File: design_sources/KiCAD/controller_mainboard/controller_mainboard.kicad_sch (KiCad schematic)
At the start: 2 parts, among them J5 XT-90, J6 USB_C_Receptacle_USB2.0_16P

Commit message: Commit after closing kicad
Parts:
- added L4: 5A 1uH, symbol Device:L
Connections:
- net at J6.A6 (D+): now also J6.B6 (D+)
- net at J6.A7 (D-): now also J6.B7 (D-)
- net at J6.S1 (SHIELD): now also L4.1
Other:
- note added: "22R resistors and MAKE THIS DIFFERENTIAL"
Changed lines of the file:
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@@
+		)
+	)
+	(text "22R resistors and MAKE THIS DIFFERENTIAL\n"
+		(exclude_from_sim no)
+		(at 59.436 118.11 0)
+		(effects
+			(font
+				(size 1.27 1.27)
+			)
+			(justify left top)
+		)
+	)
+	(wire
+		(pts
+			(xy 45.72 142.24) (xy 45.72 144.78)
+		)
+		(stroke
+			(width 0)
+			(type default)
+		)
+	)
+	(wire
+		(pts
+			(xy 45.72 144.78) (xy 43.18 144.78)
+		)
+		(stroke
+			(width 0)
+			(type default)
+		)
+	)
+	(wire
+		(pts
+			(xy 43.18 124.46) (xy 57.15 124.46)
+		)
+		(stroke
+			(width 0)
+			(type default)
+		)
+	)
+	(wire
+		(pts
+			(xy 20.32 173.99) (xy 21.59 173.99)
+		)
+		(stroke
+			(width 0)
+			(type default)
+		)
+	)
+	(wire
+		(pts
+			(xy 45.72 139.7) (xy 45.72 137.16)
+		)
+		(stroke
+			(width 0)
+			(type default)
+		)
+	)
+	(wire
+		(pts
+			(xy 20.32 162.56) (xy 20.32 173.99)
+		)
+		(stroke
+			(width 0)
+			(type default)
+		)
+	)
+	(wire
+		(pts
+			(xy 45.72 137.16) (xy 43.18 137.16)
+		)
+		(stroke
+			(width 0)
+			(type default)
+		)
+	)
+	(wire
+		(pts
+			(xy 43.18 142.24) (xy 45.72 142.24)
+		)
+		(stroke
+			(width 0)
+			(type default)
+		)
+	)
+	(wire
+		(pts
+			(xy 43.18 139.7) (xy 45.72 139.7)
+		)
+		(stroke
+			(width 0)
+			(type default)
+		)
+	)
+	(symbol
+		(lib_id "Device:L")
+		(at 25.4 173.99 90)
+		(unit 1)
+		(exclude_from_sim no)
+		(in_bom yes)
+		(on_board yes)
+		(dnp no)
+		(fields_autoplaced yes)
+		(property "Reference" "L4"
+			(at 25.4 168.91 90)
+			(effects
+				(font
+					(size 1.27 1.27)
+				)
+			)
+		)
+		(property "Value" "5A 1uH"
+			(at 25.4 171.45 90)
+			(effects
+				(font
+					(size 1.27 1.27)
+				)
+			)
+		)
+		(property "Footprint" ""
+			(at 25.4 173.99 0)
+			(effects
+				(font
+					(size 1.27 1.27)
+				)
+				(hide yes)
+			)
+		)
+		(property "Datasheet" "~"
+			(at 25.4 173.99 0)
+			(effects
+				(font
+					(size 1.27 1.27)
+				)
+				(hide yes)
+			)
+		)
+		(property "Description" "Inductor"
+			(at 25.4 173.99 0)
+			(effects
+				(font
+					(size 1.27 1.27)
+				)
+				(hide yes)
+			)
+		)
+		(property "JLCPCB" "C167953"
+			(at 25.4 173.99 90)
+			(effects
+				(font
+					(size 1.27 1.27)
+				)
+				(hide yes)
+			)
+		)
+		(pin "1"
+		)
+		(pin "2"
+		)
+		(instances
+			(project "controller_mainboard"
+				(path "/0fdfffec-3d24-4249-8ba9-dae7a6ccc250"
+					(reference "L4")
+					(unit 1)
+				)
+			)
 		)
 	)
@@
 	)
 	(sheet
-		(at 73.66 95.25)
+		(at 76.2 127)
 		(size 33.02 35.56)
 		(exclude_from_sim no)
@@
 		)
 		(property "Sheetname" "ATmega16u2"
-			(at 73.66 94.5384 0)
+			(at 76.2 126.2884 0)
 			(effects
 				(font
@@
 		)
 		(property "Sheetfile" "atmega16u2_schematic.kicad_sch"
-			(at 73.66 131.3946 0)
+			(at 76.2 163.1446 0)
 			(effects
 				(font
@@
 		)
 		(pin "PE0" output
-			(at 106.68 111.76 0)
+			(at 109.22 143.51 0)
 			(effects
 				(font
@@
 		)
 		(pin "PE1" output
-			(at 106.68 114.3 0)
+			(at 109.22 146.05 0)
 			(effects
 				(font
@@
 		)
 		(pin "RESET_CPL" input
-			(at 106.68 125.73 0)
+			(at 109.22 157.48 0)
 			(effects
 				(font
@@
 		)
 		(pin "usb_d+" input
-			(at 73.66 114.3 180)
+			(at 76.2 146.05 180)
 			(effects
 				(font
@@
 		)
 		(pin "usb_d-" input
-			(at 73.66 116.84 180)
+			(at 76.2 148.59 180)
 			(effects
 				(font
@@
 		)
 		(pin "usb_GND" passive
-			(at 73.66 119.38 180)
+			(at 76.2 151.13 180)
 			(effects
 				(font
@@
 		)
 		(pin "usb_VCC" input
-			(at 73.66 111.76 180)
-			(effects
-				(font
+			(at 76.2 143.51 180)
+			(effects
+				(font

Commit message: Populated the schematic more, added buck.
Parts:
- removed L4: 5A 1uH, symbol Device:L
- added D12: 40V 5A, Diode_SMD:D_SMA, symbol Device:D
- added D13: LED RED, LED_SMD:LED_0603_1608Metric, symbol Device:LED
- added F1: Fuse 20A, Custom_feetprint:BLX-A fuse holder, symbol Device:Fuse
- added FB1: GZ2012D101TF, Inductor_SMD:L_0805_2012Metric, symbol Device:FerriteBead
- added J10, J11, J8, J9: 2P_screw_term, symbol Connector_Generic:Conn_01x02
- added J7: XT-60, symbol Connector_Generic:Conn_01x02
- added Q5: 2N7002, Package_TO_SOT_SMD:SOT-23, symbol Transistor_FET:2N7002
- added R17, R18: 22R 100mW, Resistor_SMD:R_0603_1608Metric, symbol Device:R
- added R23: 10k 63mW, Resistor_SMD:R_0402_1005Metric, symbol Device:R
- added R24: 1k 63mW, Resistor_SMD:R_0402_1005Metric, symbol Device:R
- added R26, R27: 5.1K 100mW, Capacitor_SMD:C_0603_1608Metric, symbol Device:R
- added SW1: SW_SPDT, Custom_feetprint:MTS-10x, symbol Switch:SW_SPDT
- J6: footprint (none) -> Connector_USB:USB_C_Receptacle_GCT_USB4105-xx-A_16P_TopMnt_Horizontal; JLCPCB (none) -> C2927038
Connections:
- net at J6.S1 (SHIELD): now also FB1.1
- net at J5.1 (Pin_1): now also F1.2, J7.1 (Pin_1), R24.2
- net GND: now reaches J5.2 (Pin_2)
- net GND: now also J7.2 (Pin_2), Q5.2 (S), R23.1
- net USB_GND: now reaches J6.A1 (GND), J6.A12 (GND), J6.B1 (GND), J6.B12 (GND)
- net USB_GND: now also FB1.2, R26.2, R27.2
- net USB_VBUS: now reaches J6.A4 (VBUS), J6.A9 (VBUS), J6.B4 (VBUS), J6.B9 (VBUS)
- net USB_VBUS: now also D12.2 (A), Q5.1 (G), R23.2
- net at J6.A5 (CC1): now also R27.1
- net USB_DATA_P: now reaches J6.A6 (D+), J6.B6 (D+)
- net USB_DATA_P: now also R18.2
- net USB_DATA_N: now reaches J6.A7 (D-), J6.B7 (D-)
- net USB_DATA_N: now also R17.2
- net at J6.B5 (CC2): now also R26.1
- new net: F1.1, SW1.2 (B)
- new net: D13.2 (A), R24.1
- new net +5V: D12.1 (K)
- new net +BATT: D13.1 (K), SW1.3 (C)
- new net 5V_3A_buck_converter/BUCK_EN: Q5.3 (D)
- new net Motor driver 1/MOTOR_A: J8.1 (Pin_1)
- new net Motor driver 1/MOTOR_B: J8.2 (Pin_2)
- new net Motor driver 2/MOTOR_A: J9.1 (Pin_1)
- new net Motor driver 2/MOTOR_B: J9.2 (Pin_2)
- new net Motor driver 3/MOTOR_A: J10.1 (Pin_1)
- new net Motor driver 3/MOTOR_B: J10.2 (Pin_2)
- new net Motor driver 4/MOTOR_A: J11.1 (Pin_1)
- new net Motor driver 4/MOTOR_B: J11.2 (Pin_2)
- new net USB_D_N: R17.1
- new net USB_D_P: R18.1
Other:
- removed sheet Motor driver
- added sheet 5V_3A_buck_converter (5V5_36V_3A_buck_converter_5V.kicad_sch)
- added sheet Motor driver 1 (dc_motor_driver.kicad_sch)
- added sheet Motor driver 2 (dc_motor_driver.kicad_sch)
- added sheet Motor driver 3 (dc_motor_driver.kicad_sch)
- added sheet Motor driver 4 (dc_motor_driver.kicad_sch)
- note added: "0.8A, 100Ohm@100MHz, Rdc 150mOhm"
- note added: "5A*4 = 20A"
- note added: "CC conf marks USB2.0"
- note added: "Disable buck when usb connected"
- note added: "FLT indicator"
- note added: "Supply range: 8.5V - 15"
- note removed: "22R resistors and MAKE THIS DIFFERENTIAL"
- moved on the sheet: J5

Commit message: Continued development on the schematic. Pins wired. TODO validate.
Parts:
- added J13: 02x20_raspbi_conn, symbol Connector_Generic:Conn_02x20_Odd_Even
- added J14: Conn_01x10_2.54mm_socket, Connector_PinSocket_2.54mm:PinSocket_1x10_P2.54mm_Vertical, symbol Connector:Conn_01x10_Socket
- added J15, J17, J21, J22, J23: 01x08_2.54mm _socket, Connector_PinSocket_2.54mm:PinSocket_1x08_P2.54mm_Vertical, symbol Connector:Conn_01x08_Socket
- added J18: 02x18_2.54mm_socket, symbol Connector_Generic:Conn_02x18_Odd_Even
- added Q6: 2N7002, Package_TO_SOT_SMD:SOT-23, symbol Transistor_FET:2N7002
- added R25: 10k 63mW, Resistor_SMD:R_0402_1005Metric, symbol Device:R
- added R28: 22R 100mW, Resistor_SMD:R_0603_1608Metric, symbol Device:R
- J10, J11, J9: footprint (none) -> Connector_JST:JST_NV_B02P-NV_1x02_P5.00mm_Vertical
- J8: footprint (none) -> Connector_JST:JST_NV_B02P-NV_1x02_P5.00mm_Vertical; tinytronics (none) -> https://www.tinytronics.nl/en/cables-and-connectors/connect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
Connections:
- net +5V: now also J15.2 (Pin_2), J15.5 (Pin_5), J18.1 (Pin_1), J18.2 (Pin_2)
- net 5V_3A_buck_converter/BUCK_EN: now also Q6.3 (D)
- net GND: now also J13.14 (Pin_14), J13.20 (Pin_20), J13.25 (Pin_25), J13.30 (Pin_30), J13.34 (Pin_34), J13.39 (Pin_39), J13.6 (Pin_6), J13.9 (Pin_9), J14.4 (Pin_4), J15.6 (Pin_6), J15.7 (Pin_7), J18.35 (Pin_35), J18.36 (Pin_36), Q6.2 (S), R25.1
- new net: Q6.1 (G), R25.2, R28.1
- new net +3V3: J13.1 (Pin_1), J13.17 (Pin_17), J15.4 (Pin_4), R28.2
- new net ADC0: J21.1 (Pin_1)
- new net ADC1: J21.2 (Pin_2)
- new net ADC10: J17.3 (Pin_3)
- new net ADC11: J17.4 (Pin_4)
- new net ADC12: J17.5 (Pin_5)
- new net ADC13: J17.6 (Pin_6)
- new net ADC14: J17.7 (Pin_7)
- new net ADC15: J17.8 (Pin_8)
- new net ADC2: J21.3 (Pin_3)
- new net ADC3: J21.4 (Pin_4)
- new net ADC4: J21.5 (Pin_5)
- new net ADC5: J21.6 (Pin_6)
- new net ADC6: J21.7 (Pin_7)
- new net ADC7: J21.8 (Pin_8)
- new net ADC8: J17.1 (Pin_1)
- new net ADC9: J17.2 (Pin_2)
- new net AREF: J14.3 (Pin_3)
- new net D0: J23.8 (Pin_8)
- new net D1: J23.7 (Pin_7)
- new net D10: J14.8 (Pin_8)
- new net D11: J14.7 (Pin_7)
- new net D12: J14.6 (Pin_6)
- new net D13: J14.5 (Pin_5)
- new net D14: J22.1 (Pin_1)
- new net D15: J22.2 (Pin_2)
- new net D16: J22.3 (Pin_3)
- new net D17: J22.4 (Pin_4)
- new net D18: J22.5 (Pin_5)
- new net D19: J22.6 (Pin_6)
- new net D2: J23.6 (Pin_6)
- new net D20: J14.2 (Pin_2), J22.7 (Pin_7)
- new net D21: J14.1 (Pin_1), J22.8 (Pin_8)
- new net D22: J18.3 (Pin_3)
- new net D23: J18.4 (Pin_4)
- new net D24: J18.5 (Pin_5)
- new net D25: J18.6 (Pin_6)
- new net D26: J18.7 (Pin_7)
- new net D27: J18.8 (Pin_8)
- new net D28: J18.9 (Pin_9)
- new net D29: J18.10 (Pin_10)
- new net D3: J23.5 (Pin_5)
- new net D30: J18.11 (Pin_11)
- new net D31: J18.12 (Pin_12)
- new net D32: J18.13 (Pin_13)
- new net D33: J18.14 (Pin_14)
- new net D34: J18.15 (Pin_15)
- new net D35: J18.16 (Pin_16)
- new net D36: J18.17 (Pin_17)
- new net D37: J18.18 (Pin_18)
- new net D38: J18.19 (Pin_19)
- new net D39: J18.20 (Pin_20)
- new net D4: J23.4 (Pin_4)
- new net D40: J18.21 (Pin_21)
- new net D41: J18.22 (Pin_22)
- new net D42: J18.23 (Pin_23)
- new net D43: J18.24 (Pin_24)
- new net D44: J18.25 (Pin_25)
- new net D45: J18.26 (Pin_26)
- new net D46: J18.27 (Pin_27)
- new net D47: J18.28 (Pin_28)
- new net D48: J18.29 (Pin_29)
- new net D49: J18.30 (Pin_30)
- new net D5: J23.3 (Pin_3)
- new net D50: J18.31 (Pin_31)
- new net D51: J18.32 (Pin_32)
- new net D52: J18.33 (Pin_33)
- new net D53: J18.34 (Pin_34)
- new net D6: J23.2 (Pin_2)
- new net D7: J23.1 (Pin_1)
- new net D8: J14.10 (Pin_10)
- new net D9: J14.9 (Pin_9)
- new net RPI_GPIO0: J13.27 (Pin_27)
- new net RPI_GPIO1: J13.28 (Pin_28)
- new net RPI_GPIO10: J13.19 (Pin_19)
- new net RPI_GPIO11: J13.23 (Pin_23)
- new net RPI_GPIO12: J13.32 (Pin_32)
- new net RPI_GPIO13: J13.33 (Pin_33)
- new net RPI_GPIO14: J13.8 (Pin_8)
- new net RPI_GPIO15: J13.10 (Pin_10)
- new net RPI_GPIO16: J13.36 (Pin_36)
- new net RPI_GPIO17: J13.11 (Pin_11)
- new net RPI_GPIO18: J13.12 (Pin_12)
- new net RPI_GPIO19: J13.35 (Pin_35)
- new net RPI_GPIO2: J13.3 (Pin_3)
- new net RPI_GPIO20: J13.38 (Pin_38)
- new net RPI_GPIO21: J13.40 (Pin_40)
- new net RPI_GPIO22: J13.15 (Pin_15)
- new net RPI_GPIO23: J13.16 (Pin_16)
- new net RPI_GPIO24: J13.18 (Pin_18)
- new net RPI_GPIO25: J13.22 (Pin_22)
- new net RPI_GPIO26: J13.37 (Pin_37)
- new net RPI_GPIO27: J13.13 (Pin_13)
- new net RPI_GPIO3: J13.5 (Pin_5)
- new net RPI_GPIO4: J13.7 (Pin_7)
- new net RPI_GPIO5: J13.29 (Pin_29)
- new net RPI_GPIO6: J13.31 (Pin_31)
- new net RPI_GPIO7: J13.26 (Pin_26)
- new net RPI_GPIO8: J13.24 (Pin_24)
- new net RPI_GPIO9: J13.21 (Pin_21)
- new net ~{mega2560_reset}: J15.3 (Pin_3)
- no-connect marks 0 -> 2
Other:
- added sheet Quadrature encoder 1 (qdec_pullup.kicad_sch)
- added sheet Quadrature encoder 2 (qdec_pullup.kicad_sch)
- added sheet Quadrature encoder 3 (qdec_pullup.kicad_sch)
- added sheet Quadrature encoder 4 (qdec_pullup.kicad_sch)
- sheet atmega2560 ports: added ADC0, ADC1, ADC10, ADC11, ADC12, ADC13, ADC14, ADC15, ADC2, ADC3, ADC4, ADC5, ADC6, ADC7, ADC8, ADC9, AREF, PA0/D22, PA1/D23, PA2/D24, PA3/D25, PA4/D26, PA5/D27, PA6/D28, PA7/D29, PB0/D55/SS, PB1/D52/SCK, PB2/D51/MOSI, PB3/D50/MISO, PB4/D10, PB5/D11, PB6/D12, PB7/D13, PC0/D37, PC1/D36, PC2/D35, PC3/D34, PC4/D33, PC5/D32, PC6/D31, PC7/D30, PD0/D21/SCL, PD1/D20/SDA, PD2/D19/RXD1, PD3/D18/TXD1, PD7/D38, PE0/D0/RX0, PE1/D1/TX0, PE3/D5, PE4/D2, PE5/D3, PG0/D41, PG1/D40, PG2/D39, PG5/D4, PH0/D17/RXD2, PH1/D16/TXD2, PH3/D6, PH4/D7, PH5/D8, PH6/D9, PL0/D49, PL1/D48, PL2/D47, PL3/D46, PL4/D45, PL5/D44, PL6/D43, PL7/D42, RXD3, TXD3, ~{RESET}; removed none
- note added: "All raspbi after B+ can provide up to 500mA on 3v3."
- note added: "Didn't the TETRIX motor have JST? They have a 2mm pitch jst type connector. Probably PH The motor has 4P male side."
- note added: "Does rasbpi want to PWM control?"
- note added: "FLT/OPEN indicator"
- note added: "Get these from Tinytronics to interface the encoders with the PCB: JST-PH Female to DuPont Female Compatible Cable - 4p - 15cm SKU:005974 https://www.tinytronics.nl/en/cables-and-connectors/cables-and-adapters/jst-compatible/jst-ph-female-to-dupont-female-compatible-cable-4p-15cm"
- note added: "Raspi 5V supply"
- note added: "TODO VALIDATE"
- note added: "TODO, check if we can change this flag into something like V_PERIPHERAL So that it can be swapped with 5V or 3V3"
- note added: "TODOS - CHECK if 5v buck can handle external 5v supply while disabled. - place esd parts - Selectable peripheral voltage 3.3V/5V for enc control"
- note removed: "FLT indicator"
- company: Kestech -> Mete Han Keskin
- moved on the sheet: D12, FB1, J10, J11, J6, J8, J9, Q5, R17, R18, R23, R26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

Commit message: Added ESD protection ic, added footprints to all IC and loaded into pcbnew to size up the pcb size.
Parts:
- added U12: USBLC6-4SC6, Package_TO_SOT_SMD:SOT-23-6, symbol Power_Protection:USBLC6-4SC6
- J1: renamed from J5; footprint (none) -> Custom_feetprint:XT-90_Connector
- J15: renamed from J13; footprint (none) -> Connector_PinHeader_2.54mm:PinHeader_2x20_P2.54mm_Vertical
- J2: renamed from J7; footprint (none) -> Connector_AMASS:AMASS_XT60-M_1x02_P7.20mm_Vertical
- J7: renamed from J18; footprint (none) -> Connector_PinHeader_2.54mm:PinHeader_2x18_P2.54mm_Vertical
- renumbered D13 to D1, D12 to D2, J22 to J10, J8 to J11, J9 to J12, J10 to J13, J11 to J14, J6 to J3, J15 to J4, J21 to J5, J17 to J6, J14 to J8, J23 to J9, Q5 to Q1, Q6 to Q2, R23 to R1, R28 to R2, R25 to R3, R24 to R4, R27 to R5, R26 to R6, R17 to R7, R18 to R8
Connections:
- net USB_DATA_N: now also U12.3 (I/O2)
- net USB_DATA_P: now also U12.1 (I/O1)
- net USB_GND: now also U12.2 (GND)
- net USB_VBUS: now also U12.5 (VBUS)
- net at J3.B5 (CC2), R6.1: now also U12.4 (I/O3)
- net at J3.A5 (CC1), R5.1: now also U12.6 (I/O4)
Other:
- note added: "ESD stuff DFN1006 single C22395519 LSR05-TP C779191 HELL YEAh C778952 mex dfn16"
- note added: "PERFECT!!! USBLC6-4SC6-ES C5180279 SEUC10F5V4U C5126804 IP4220CZ6-ES C5199235"
- note added: "Single channel esd protect ESD5V0AP C5199224"
- moved on the sheet: D2, FB1, J10, J11, J12, J13, J14, J4, J5, J6, J7, J8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

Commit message: Read through schematic to bugfix.
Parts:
- removed Q2: 2N7002, Package_TO_SOT_SMD:SOT-23, symbol Transistor_FET:2N7002
- removed R2: 22R 100mW, Resistor_SMD:R_0603_1608Metric, symbol Device:R
- removed R3: 10k 63mW, Resistor_SMD:R_0402_1005Metric, symbol Device:R
- added C91: 50V 100nF X7R, Capacitor_SMD:C_0603_1608Metric, symbol Device:C
- added D36: LED GREEN, LED_SMD:LED_0805_2012Metric, symbol Device:LED
- added J24: XT-60, Connector_AMASS:AMASS_XT60-M_1x02_P7.20mm_Vertical, symbol Connector_Generic:Conn_01x02
- added R62, R63: 1k 63mW, Resistor_SMD:R_0402_1005Metric, symbol Device:R
- added R80: 5.1K 100mW, Capacitor_SMD:C_0603_1608Metric, symbol Device:R
- added R81: 10k 63mW, Resistor_SMD:R_0402_1005Metric, symbol Device:R
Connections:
- net +5V: now also R62.1, R63.1
- net +BATT: now also J24.2 (Pin_2), R81.2
- net GND: now also J1.1 (Pin_1), J2.1 (Pin_1), C91.1, D36.1 (K), J24.1 (Pin_1), R80.1; no longer J1.2 (Pin_2), J2.2 (Pin_2)
- net at J3.B5 (CC2), R6.1: no longer U12.4 (I/O3)
- net at J3.A5 (CC1), R5.1: no longer U12.6 (I/O4)
- net at F1.2, R4.2: now also J1.2 (Pin_2), J2.2 (Pin_2); no longer J1.1 (Pin_1), J2.1 (Pin_1)
- new net: D36.2 (A), R62.2, R63.2
- new net VBAT_ADC: C91.2, R80.2, R81.1
- no-connect marks 2 -> 4
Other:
- removed sheet Motor back EMF arrestor
- sheet 5V_3A_buck_converter ports: added BUCK_5V_OUT; removed BUCK_5V_3A_OUT
- sheet ATmega16u2 ports: added RXD/PROG, TXD/PROG; removed PE0, PE1
- note added: "5V at 15Vbat"
- note added: "Additional BACK emf clamping connector. Start clamp at 14V-15V. Needed when heavy motors are used that actively brake."
- note added: "TODO: Does rasbpi want to PWM control? If so, parallel connect pins Does raspi want ENC data? If so, change ENC supply to 3v3 Does raspbi want to be able to read analog currents? Add ADC perpheral Proposed easy solution: Write ardu mega code to report data through serial, and accept commands through serial. (Good HW abstraction practice)"
- note removed: "Battery voltage range: 10.2 - 12.6 DC jack in. USB-PD supply?"
- note removed: "Does rasbpi want to PWM control?"
- note removed: "TODOS - CHECK if 5v buck can handle external 5v supply while disabled. - place esd parts - Selectable peripheral voltage 3.3V/5V for enc control"
- moved on the sheet: J1, J2

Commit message: Adjusted gitignore to ignore backups, removed backup files
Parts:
- removed J15: 02x20_raspbi_conn, Connector_PinHeader_2.54mm:PinHeader_2x20_P2.54mm_Vertical, symbol Connector_Generic:Conn_02x20_Odd_Even
- removed SW1: SW_SPDT, Custom_feetprint:MTS-10x, symbol Switch:SW_SPDT
- added J25: XT-60, Connector_AMASS:AMASS_XT60-M_1x02_P7.20mm_Vertical, symbol Connector_Generic:Conn_01x02
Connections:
- net +BATT: now also J25.1 (Pin_1)
- net at F1.1: now also J25.2 (Pin_2)
- net +3V3: no longer names the net of J4.4 (Pin_4)
- no-connect marks 4 -> 21
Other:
- sheet atmega2560 ports: added PB0/D53/SS; removed PB0/D55/SS
- note added: "Emergency stop connector"
- note added: "TODO connect these"
- note removed: "Raspi 5V supply"
- moved on the sheet: D36, R62, R63

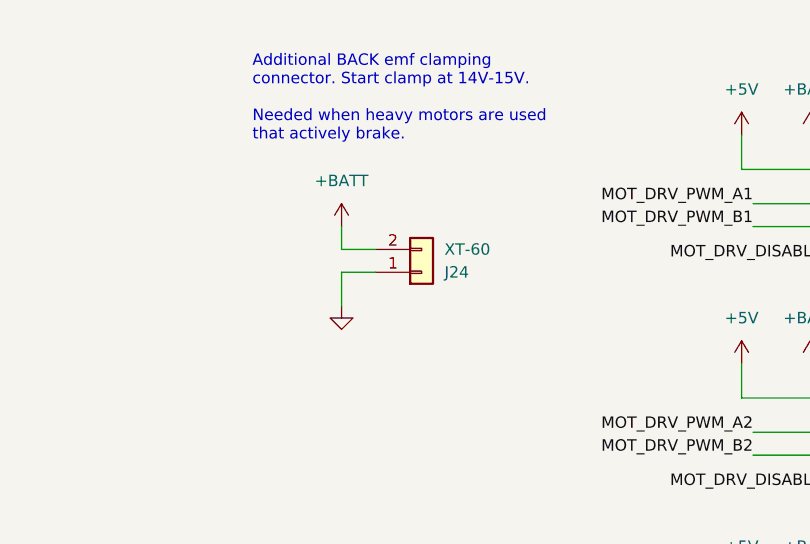
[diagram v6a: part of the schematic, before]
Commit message: Removed backups again, improved the PCB layout
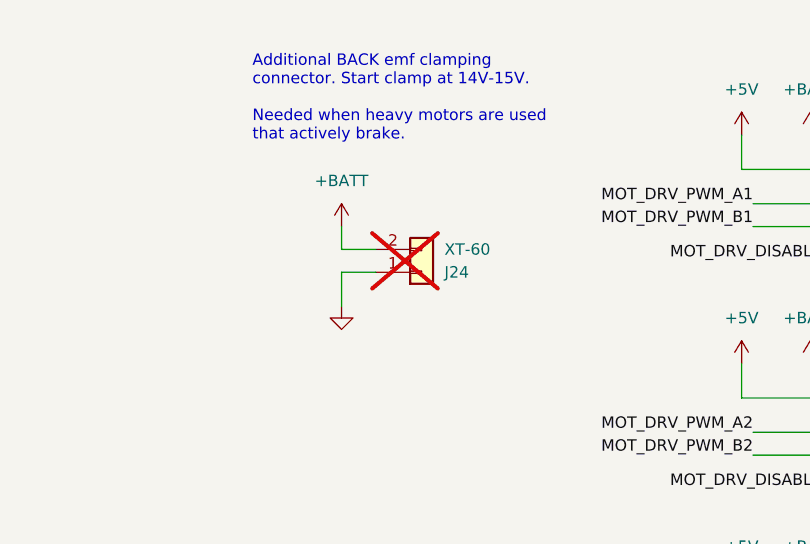
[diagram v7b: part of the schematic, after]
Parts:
- J24: now not fitted
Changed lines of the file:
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@@
 		(in_bom yes)
 		(on_board yes)
-		(dnp no)
+		(dnp yes)
 		(property "Reference" "J24"
 			(at 214.63 46.9901 0)
